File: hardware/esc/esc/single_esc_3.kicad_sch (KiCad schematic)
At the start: 41 parts, among them Q1 Q_NMOS, Q2 Q_NMOS, Q3 Q_NMOS, Q4 Q_NMOS, Q5 Q_NMOS, Q6 Q_NMOS, U1 NSG2065Q, U2 AT32F421G8U7

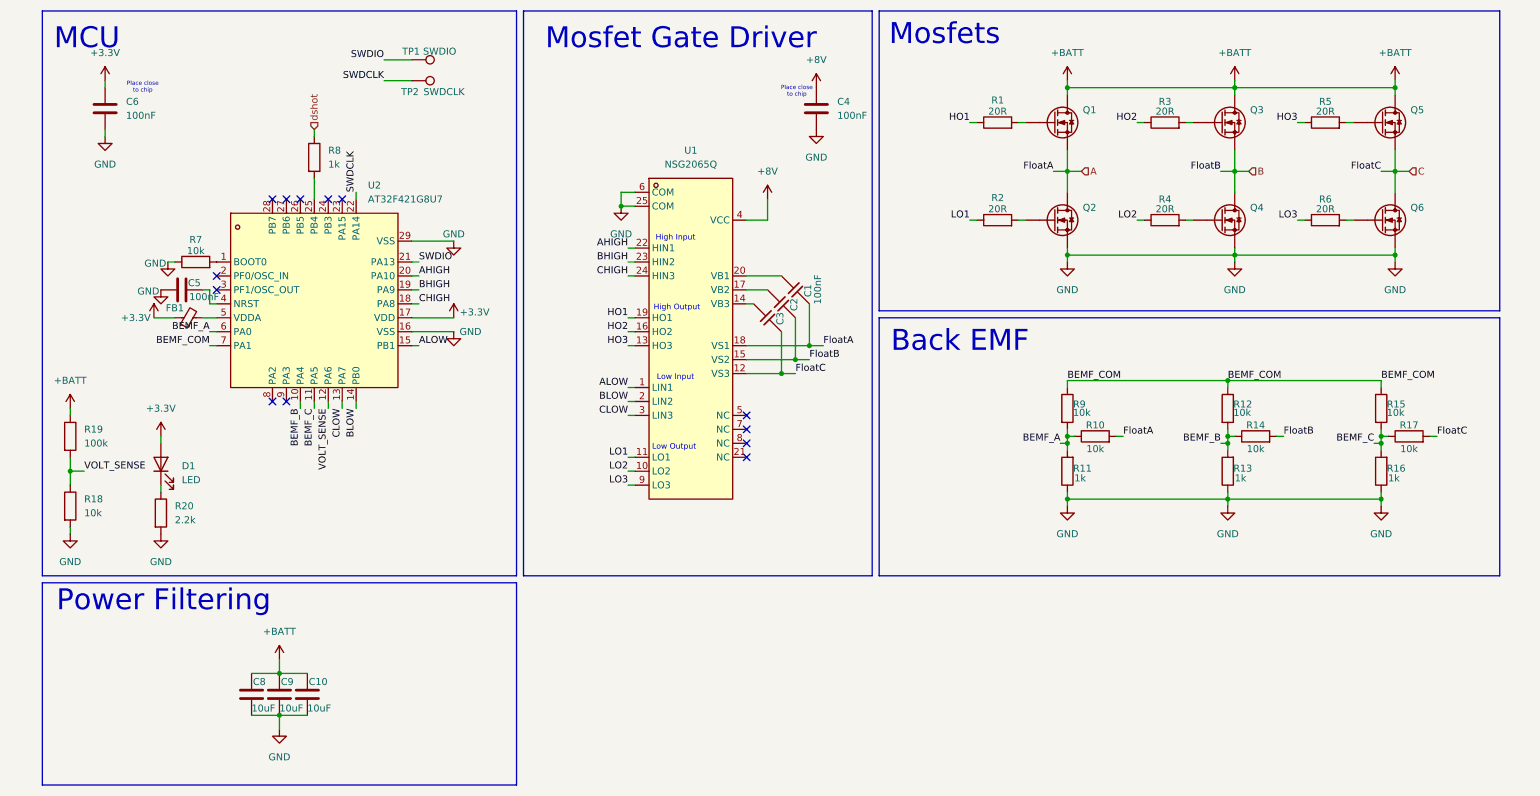
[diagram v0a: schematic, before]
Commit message: board pcb + res arrays
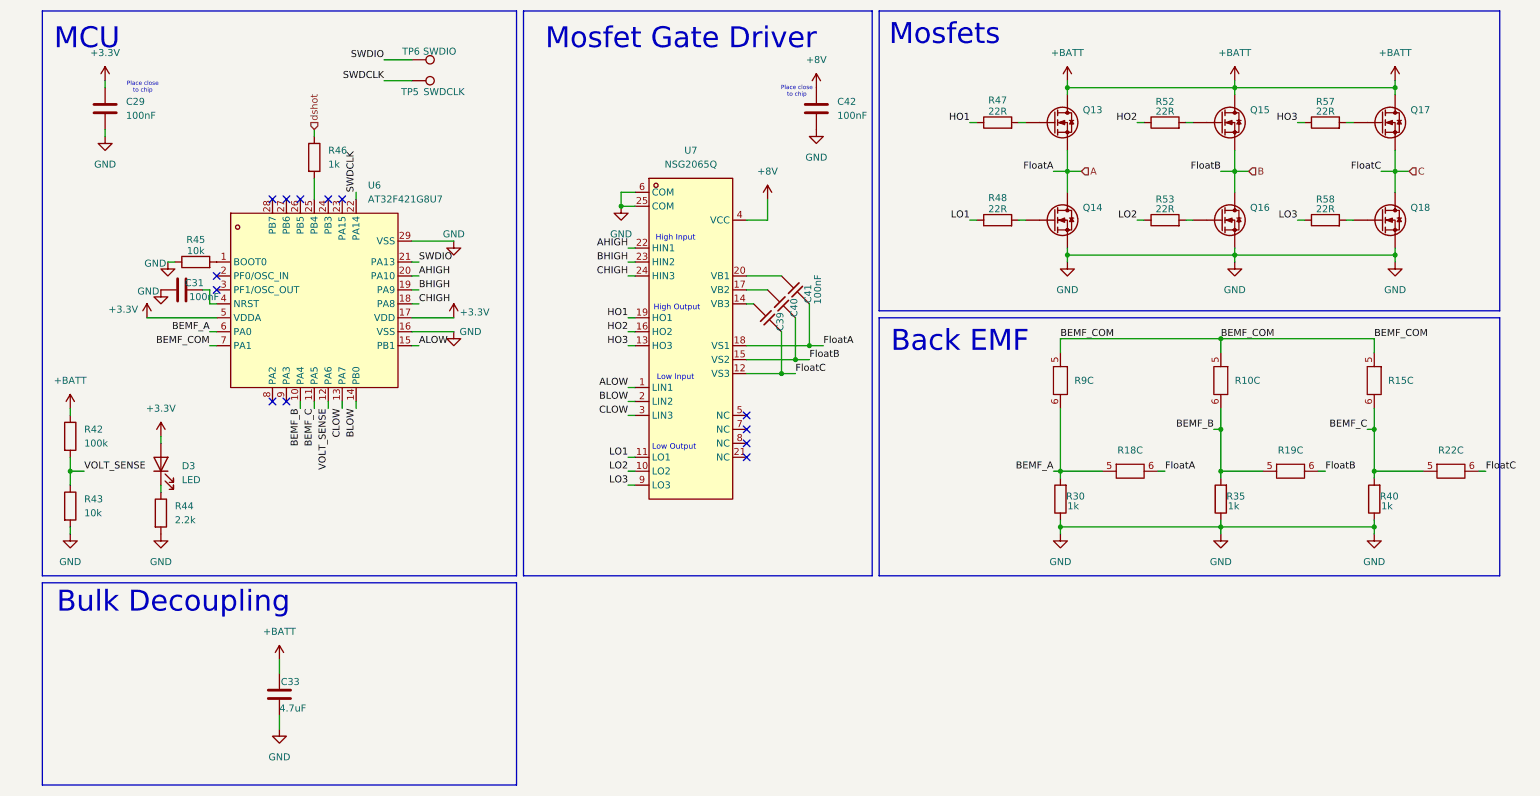
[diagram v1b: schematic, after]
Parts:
- removed C10, C8: 10uF, Capacitor_SMD:C_0603_1608Metric, symbol Device:C
- removed FB1: FerriteBead_Small, Resistor_SMD:R_0805_2012Metric, symbol Device:FerriteBead_Small
- removed R10, R12, R14, R15, R17, R9: 10k, Resistor_SMD:R_0603_1608Metric, symbol Device:R
- removed R11, R13, R16: 1k, Resistor_SMD:R_0402_1005Metric, symbol Device:R
- added R10, R15, R18, R19, R22, R9: (no value), R_Pack4:RES_4D03_0603_3P2X1P6_ROH, symbol R_PACK4:R
- added R30, R35, R40: 1k, Resistor_SMD:R_0402_1005Metric, symbol Device:R
- C33: renamed from C9; value 10uF -> 4.7uF
- R43: renamed from R18; footprint Resistor_SMD:R_0603_1608Metric -> Resistor_SMD:R_0402_1005Metric
- R45: renamed from R7; footprint Resistor_SMD:R_0603_1608Metric -> Resistor_SMD:R_0402_1005Metric
- R47: renamed from R1; value 20R -> 22R; footprint Resistor_SMD:R_0603_1608Metric -> Resistor_SMD:R_0402_1005Metric
- R48: renamed from R2; value 20R -> 22R; footprint Resistor_SMD:R_0603_1608Metric -> Resistor_SMD:R_0402_1005Metric
- R52: renamed from R3; value 20R -> 22R; footprint Resistor_SMD:R_0603_1608Metric -> Resistor_SMD:R_0402_1005Metric
- R53: renamed from R4; value 20R -> 22R; footprint Resistor_SMD:R_0603_1608Metric -> Resistor_SMD:R_0402_1005Metric
- R57: renamed from R5; value 20R -> 22R; footprint Resistor_SMD:R_0603_1608Metric -> Resistor_SMD:R_0402_1005Metric
- R58: renamed from R6; value 20R -> 22R; footprint Resistor_SMD:R_0603_1608Metric -> Resistor_SMD:R_0402_1005Metric
- renumbered C6 to C29, C5 to C31, C3 to C39, C2 to C40, C1 to C41, C4 to C42, D1 to D3, Q1 to Q13, Q2 to Q14, Q3 to Q15, Q4 to Q16, Q5 to Q17, Q6 to Q18, R19 to R42, R20 to R44, R8 to R46, TP2 to TP5, TP1 to TP6, U2 to U6, U1 to U7
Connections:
- net +3.3V: now also U6.5 (VDDA)
- net A: now also R18.6
- net B: now also R19.6
- net BEMF_A: now also R18.5, R30.2, R9.6
- net BEMF_B: now also R10.6, R19.5, R35.2
- net BEMF_C: now also R15.6, R22.5, R40.2
- net BEMF_COM: now also R10.5, R15.5, R9.5
- net C: now also R22.6
- net GND: now also R30.1, R35.1, R40.1
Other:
- note added: "Bulk Decoupling"
- note removed: "Power Filtering"

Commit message: Routing done!
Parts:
- removed D3: LED, LED_SMD:LED_0603_1608Metric, symbol Device:LED
- removed R44: 2.2k, Resistor_SMD:R_0402_1005Metric, symbol Device:R
- renumbered R9 to R10, R18 to R10, R10 to R18, R19 to R18, R15 to R18, R22 to R18
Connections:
- net A: now also R10.8; no longer R10.6
- net B: now also R18.8; no longer R18.6
- net BEMF_A: now also R10.7; no longer R10.5
- net BEMF_B: now also R18.4, R18.7; no longer R18.5, R18.6
- net BEMF_C: now also R18.2; no longer R18.6
- net BEMF_COM: now also R18.1, R18.3; no longer R18.5, R18.5
